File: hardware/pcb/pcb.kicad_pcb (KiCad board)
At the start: 2 copper layers, 65 x 140 mm, 39 parts, among them Q1 FQD50N06, Q2 FQD50N06

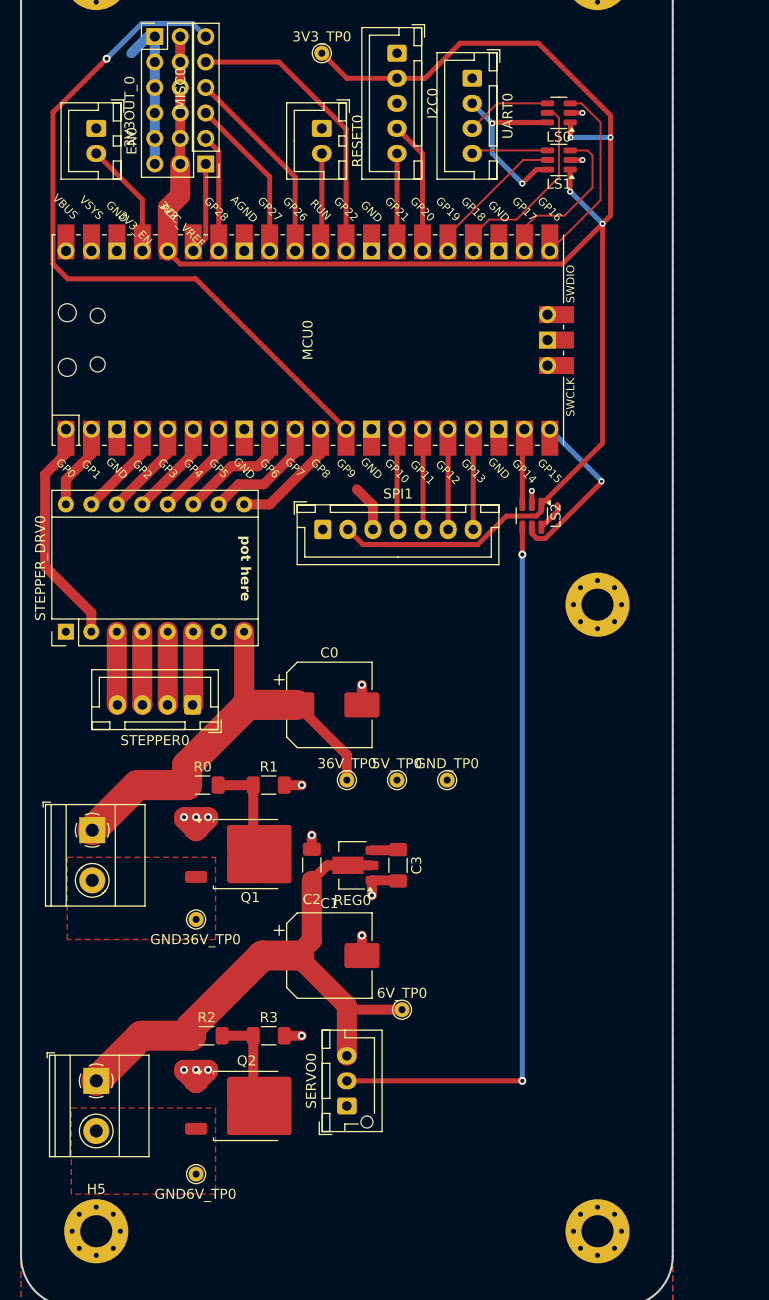
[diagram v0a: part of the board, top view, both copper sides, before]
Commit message: added silkscreen text, this board is too large though
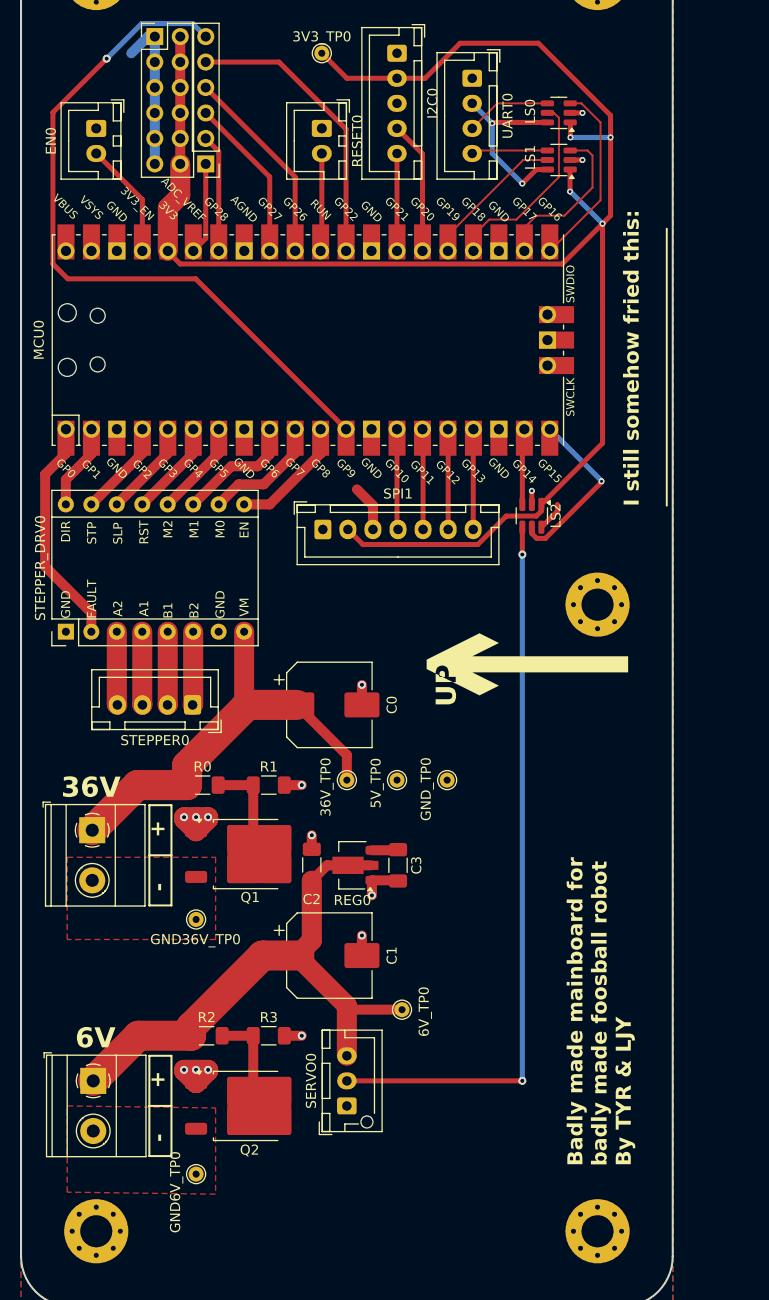
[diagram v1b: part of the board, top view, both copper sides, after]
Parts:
- moved 6VIN_0 0.30 mm to (57.2, 157.5)
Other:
- board text added: "+"
- board text added: "-"
- board text added: "36V"
- board text added: "6V"
- board text added: "A1"
- board text added: "A2"
- board text added: "B1"
- board text added: "B2"
- board text added: "Badly made mainboard for badly made foosball robot By TYR & LJY"
- board text added: "DIR"
- board text added: "EN"
- board text added: "FAULT"
- board text added: "GND"
- board text added: "I still somehow fried this: ___________________________"
- board text added: "INSULATE THESE PINS!!!! They contact the extrusion. It will short."
- board text added: "M0"
- board text added: "M1"
- board text added: "M2"
- board text added: "Probably would have been smaller if made double sided. Nothing to see here."
- board text added: "RST"
- board text added: "SLP"
- board text added: "STP"
- board text added: "UP"
- board text added: "VM"
- board text added: "Why did you take me off :("
- board text added: "↑"
- board text removed: "pot here"

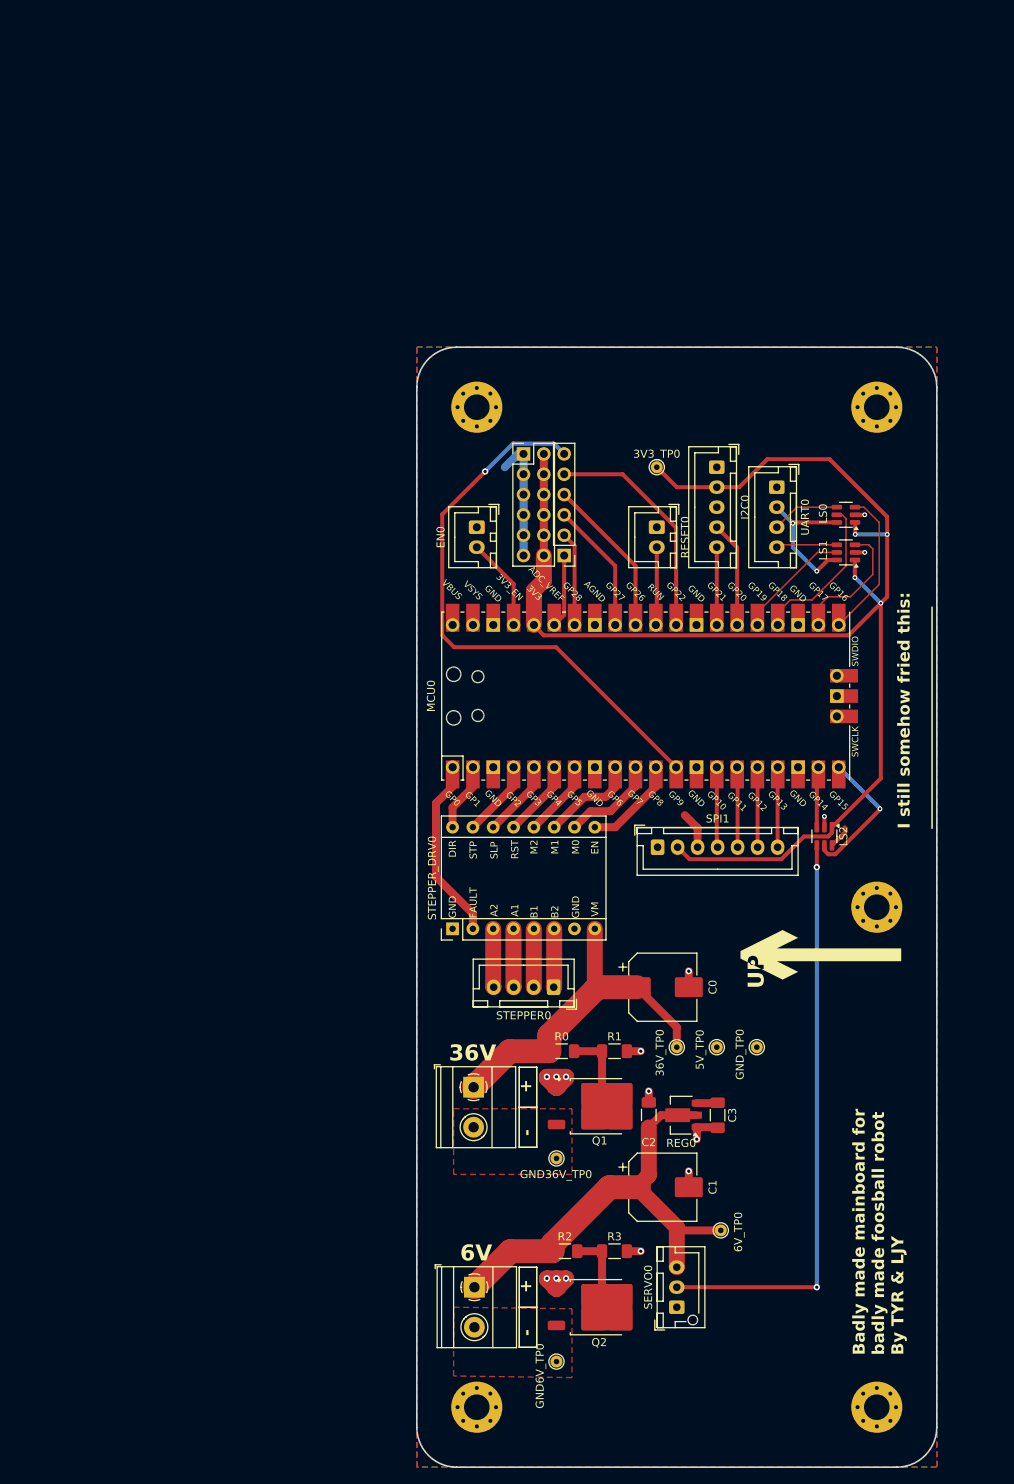
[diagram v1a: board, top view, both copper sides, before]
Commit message: made dimensions jlcpcb cheap pcb friendly
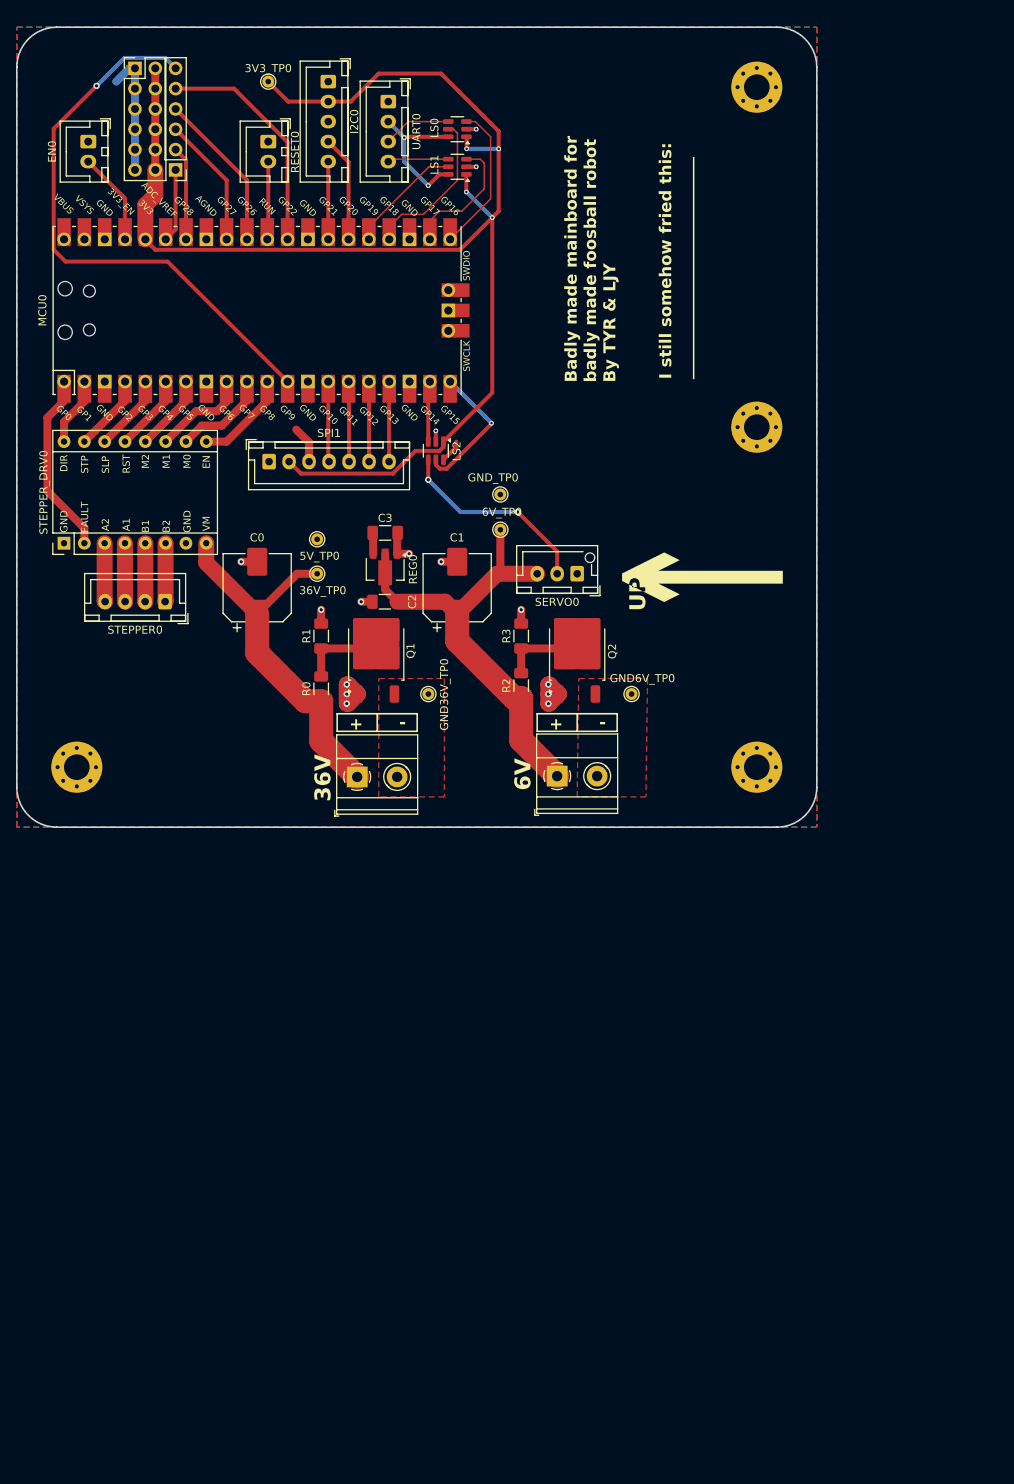
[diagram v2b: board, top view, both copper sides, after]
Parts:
- removed H5: MountingHole_Pad, MountingHole:MountingHole_3.2mm_M3_Pad_Via
- moved H4 128.1 mm to (7.50, 92.5)
- moved SERVO0 92.5 mm to (70.0, 68.3), turned to 180 degrees
- moved 6V_TP0 91.8 mm to (60.4, 62.8), turned to 90 degrees
- moved GND6V_TP0 84.0 mm to (76.8, 83.4), turned to 0 degrees
- moved C3 83.8 mm to (46.0, 63.2), turned to 0 degrees
- moved Q2 81.7 mm to (70.0, 78.3), turned to 90 degrees
- moved 5V_TP0 80.8 mm to (37.5, 64.0), turned to 90 degrees
- moved C1 79.2 mm to (55.0, 70.1), turned to 90 degrees
- moved R3 77.8 mm to (63.0, 76.1), turned to 90 degrees
- moved REG0 77.6 mm to (46.0, 67.8), turned to -90 degrees
- moved GND_TP0 76.2 mm to (60.4, 58.4), turned to -90 degrees
- moved 36V_TP0 74.3 mm to (37.5, 68.3), turned to 90 degrees
- moved C2 72.1 mm to (46.0, 71.8), turned to 180 degrees
- moved C0 71.2 mm to (30.0, 70.1), turned to 90 degrees
- moved R2 70.9 mm to (63.0, 82.3), turned to 90 degrees
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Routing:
- net /SERVO_5V: track 72.7 -> 25.1 mm
- net +36V: track 43.9 -> 47.7 mm
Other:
- board size 65 x 140 mm -> 100 x 100 mm
- board text added: "Why isnt it double sided? I dunno. Nothing to see here."
- board text removed: "INSULATE THESE PINS!!!! They contact the extrusion. It will short."
- board text removed: "Probably would have been smaller if made double sided. Nothing to see here."

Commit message: added some funny text
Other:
- board text added: "By TYR & LJY"
- board text added: "FOOSBOARD V0.1"
- board text added: "plug it in the wrong way :D"
- board text removed: "Badly made mainboard for badly made foosball robot By TYR & LJY"
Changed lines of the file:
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@@
 		)
 	)
-	(gr_text "Badly made mainboard for\nbadly made foosball robot\nBy TYR & LJY"
+	(gr_text "By TYR & LJY"
 		(at 75 44.4 90)
 		(layer "F.SilkS")
@@
 		)
 	)
+	(gr_text "FOOSBOARD V0.1"
+		(at 71.8 44.8 90)
+		(layer "F.SilkS")
+		(effects
+			(font
+				(size 3 3)
+				(thickness 0.5)
+				(bold yes)
+			)
+			(justify left bottom)
+		)
+	)
 	(gr_text "M2"
 		(at 16.6318 55.2 90)
@@
 		)
 	)
+	(gr_text "plug it in the\nwrong way :D"
+		(at 34 97.6 90)
+		(layer "F.SilkS")
+		(effects
+			(font
+				(size 1.5 1.5)
+				(thickness 0.3)
+			)
+			(justify left bottom)
+		)
+	)

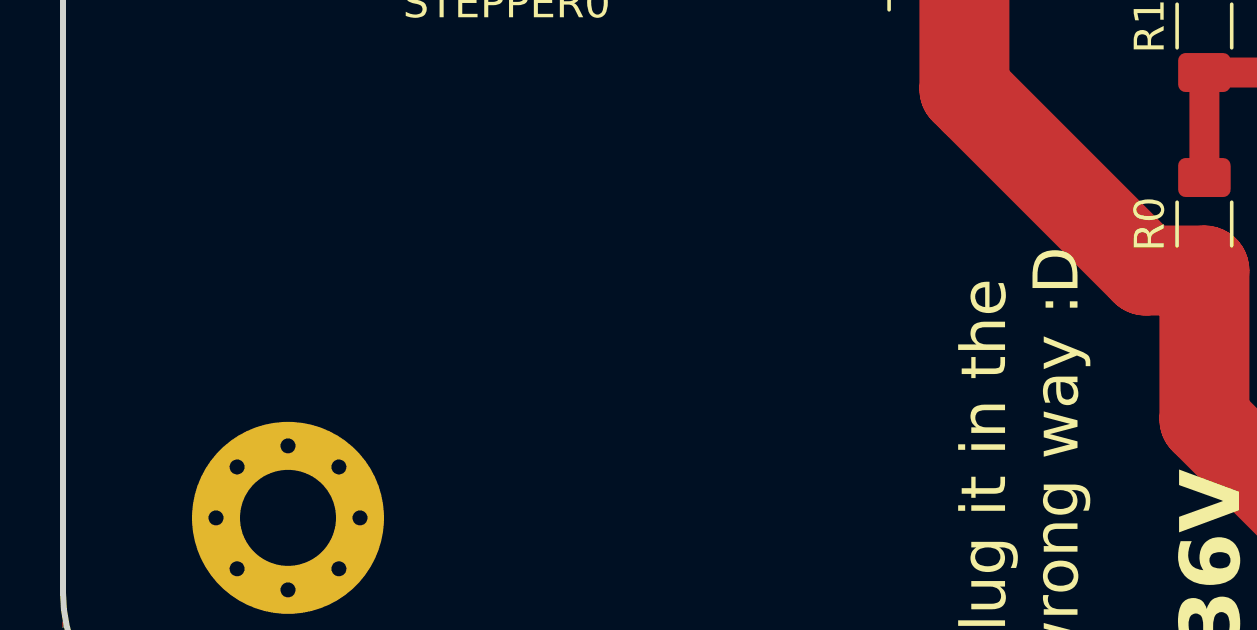
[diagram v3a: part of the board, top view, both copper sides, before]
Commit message: added and changed some more text
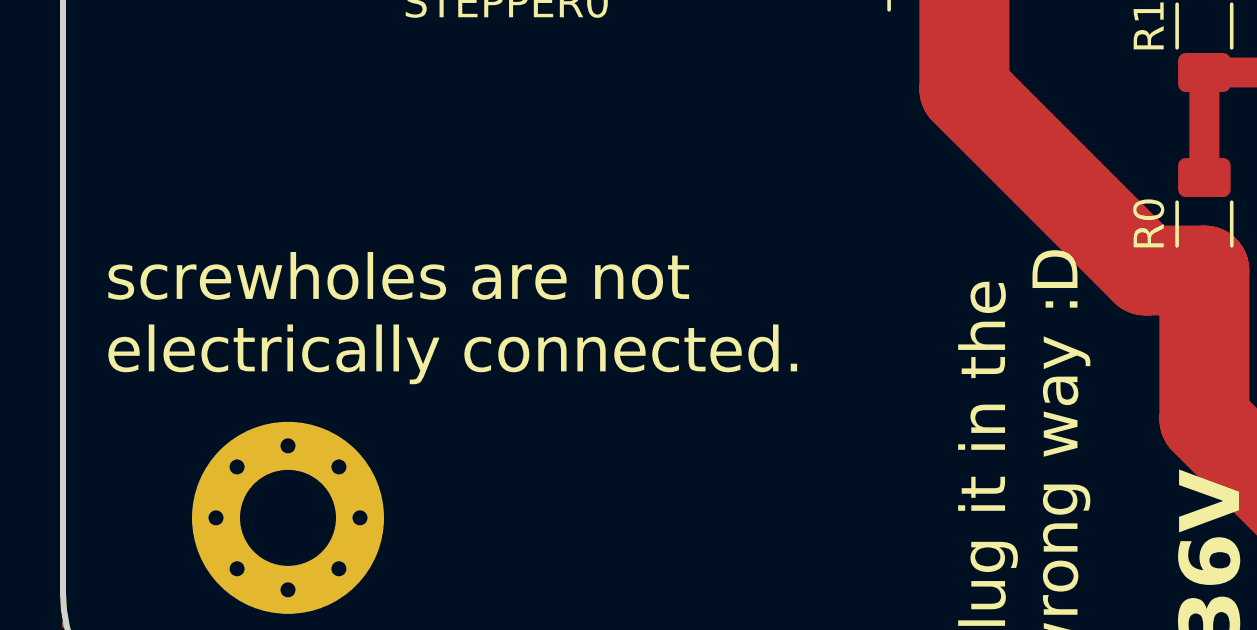
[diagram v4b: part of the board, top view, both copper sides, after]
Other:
- board text added: "Why did you take me off :( Did you fry me..."
- board text added: "screwholes are not electrically connected."
- board text removed: "Why did you take me off :("
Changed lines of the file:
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@@
 		)
 	)
-	(gr_text "Why did you take me off :("
-		(at 95.4 13 90)
+	(gr_text "Why did you take me off :(\nDid you fry me..."
+		(at 94.6 13 90)
 		(layer "B.SilkS")
 		(effects
@@
 			)
 			(justify left bottom)
+		)
+	)
+	(gr_text "screwholes are not\nelectrically connected."
+		(at 1.4 87.8 0)
+		(layer "F.SilkS")
+		(effects
+			(font
+				(size 1.5 1.5)
+				(thickness 0.3)
+			)
+			(justify left bottom)
